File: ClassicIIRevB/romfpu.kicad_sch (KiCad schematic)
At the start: 9 parts, among them J10 ROM/FPU EXPANSION SLOT, J13 PROM select

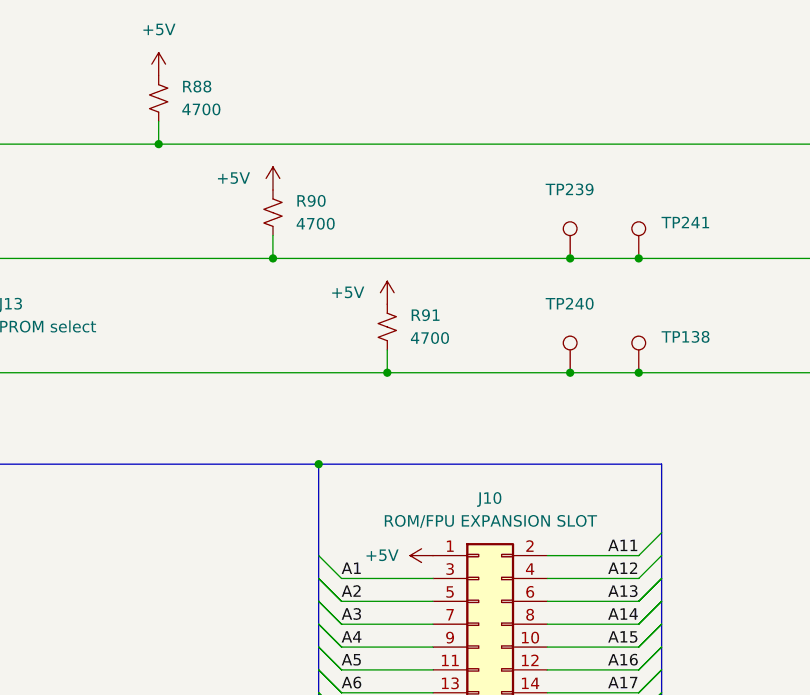
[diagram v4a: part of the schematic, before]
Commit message: Corrections to SMDs, more improved footprints
The later revision board reproduction design is now complete.
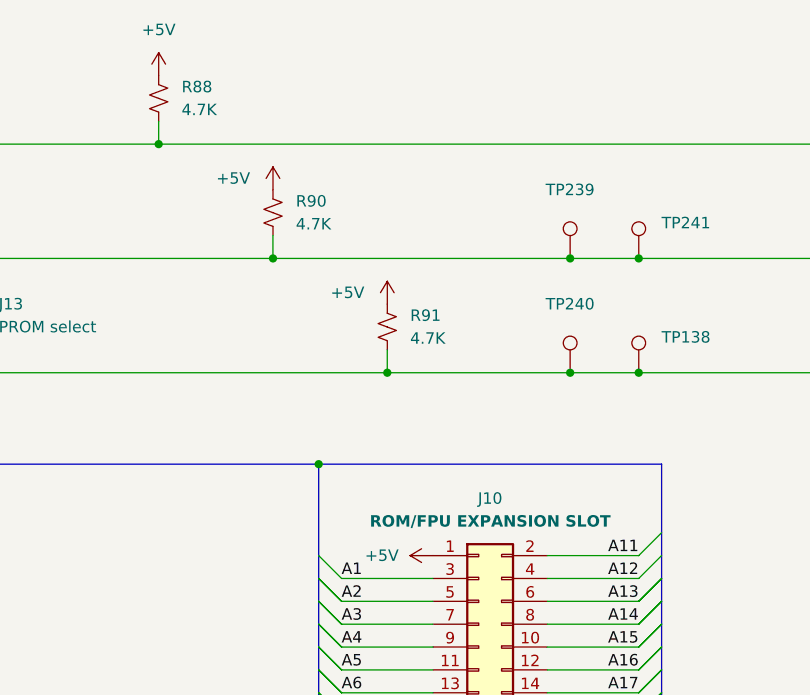
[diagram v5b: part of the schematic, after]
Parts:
- R88, R90, R91: value 4700 -> 4.7K
- TP138, TP239, TP240, TP241: now left out of the parts list
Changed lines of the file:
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@@
 	(title_block
 		(title "Macintosh Classic II (Later Revision)")
-		(date "2025-06-16")
+		(date "2025-06-21")
 		(company "Apple Computer")
 		(comment 1 "drawn by Bradley Bell")
@@
 				(font
 					(size 1.27 1.27)
+					(thickness 0.254)
+					(bold yes)
 				)
 			)
@@
 		(unit 1)
 		(exclude_from_sim no)
-		(in_bom yes)
+		(in_bom no)
 		(on_board yes)
 		(dnp no)
@@
 			)
 		)
-		(property "Value" "4700"
+		(property "Value" "4.7K"
 			(at 129.54 62.2299 0)
 			(effects
@@
 		(unit 1)
 		(exclude_from_sim no)
-		(in_bom yes)
+		(in_bom no)
 		(on_board yes)
 		(dnp no)
@@
 			)
 		)
-		(property "Value" "4700"
+		(property "Value" "4.7K"
 			(at 116.84 49.5299 0)
 			(effects
@@
 			)
 		)
-		(property "Value" "4700"
+		(property "Value" "4.7K"
 			(at 104.14 36.8299 0)
 			(effects
@@
 		(unit 1)
 		(exclude_from_sim no)
-		(in_bom yes)
+		(in_bom no)
 		(on_board yes)
 		(dnp no)
@@
 		(unit 1)
 		(exclude_from_sim no)
-		(in_bom yes)
+		(in_bom no)
 		(on_board yes)
 		(dnp no)

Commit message: Fix zones
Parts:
- J13: footprint Connector_PinHeader_2.54mm:PinHeader_2x03_P2.54mm_Vertical -> Connector_Mine:PinHeader_2x03_P2.54mm_Vertical
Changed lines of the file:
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@@
 	(title_block
 		(title "Macintosh Classic II (Later Revision)")
-		(date "2025-06-21")
+		(date "2025-06-23")
 		(company "Apple Computer")
 		(comment 1 "drawn by Bradley Bell")
@@
 			)
 		)
-		(property "Footprint" "Connector_PinHeader_2.54mm:PinHeader_2x03_P2.54mm_Vertical"
+		(property "Footprint" "Connector_Mine:PinHeader_2x03_P2.54mm_Vertical"
 			(at 78.74 58.42 0)
 			(effects
